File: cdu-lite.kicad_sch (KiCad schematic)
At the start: 0 parts

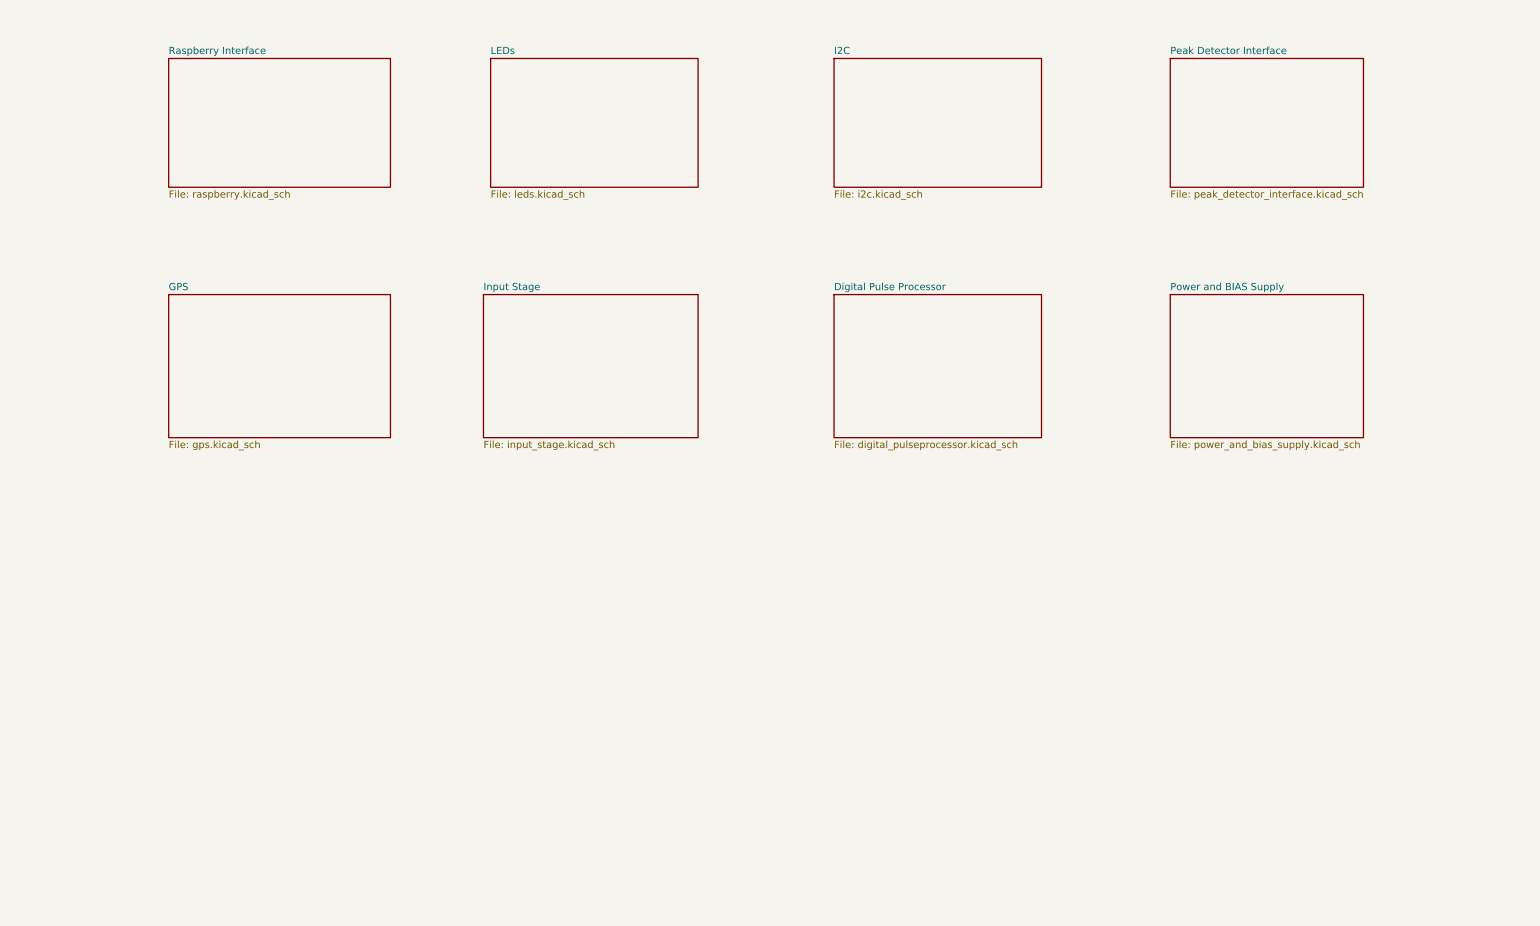
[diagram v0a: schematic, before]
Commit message: Refactored schematic to better show relationship in main schematic
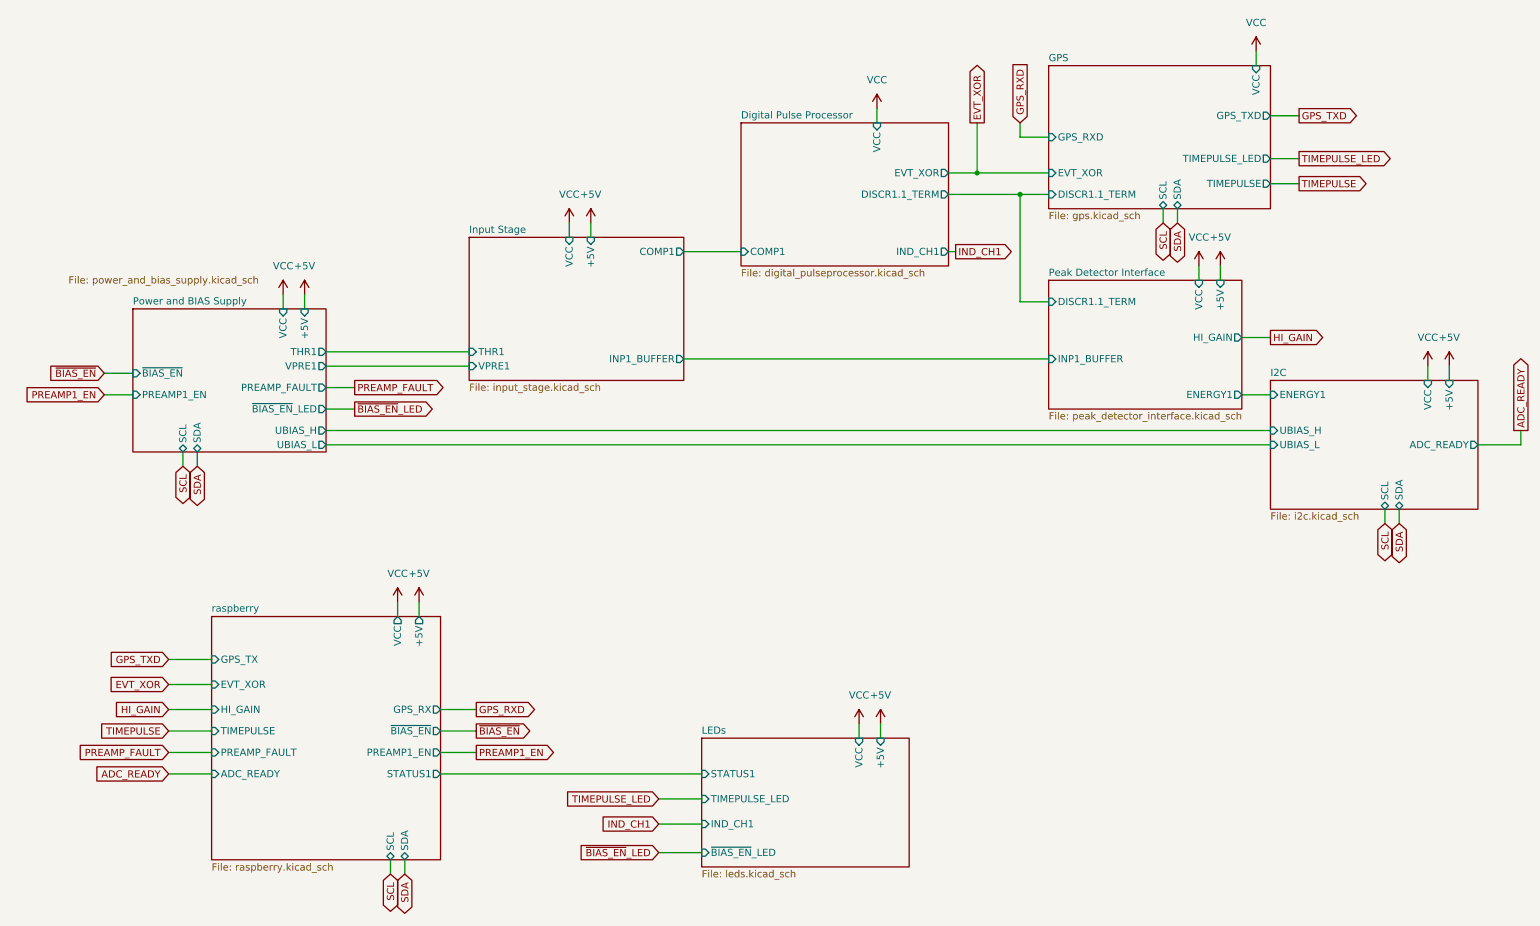
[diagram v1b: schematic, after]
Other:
- removed sheet Raspberry Interface
- added sheet raspberry (raspberry.kicad_sch)
- sheet Digital Pulse Processor ports: added COMP1, DISCR1.1_TERM, EVT_XOR, IND_CH1, VCC; removed none
- sheet GPS ports: added DISCR1.1_TERM, EVT_XOR, GPS_RXD, GPS_TXD, SCL, SDA, TIMEPULSE, TIMEPULSE_LED, VCC; removed none
- sheet I2C ports: added +5V, ADC_READY, ENERGY1, SCL, SDA, UBIAS_H, UBIAS_L, VCC; removed none
- sheet Input Stage ports: added +5V, COMP1, INP1_BUFFER, THR1, VCC, VPRE1; removed none
- sheet LEDs ports: added +5V, IND_CH1, STATUS1, TIMEPULSE_LED, VCC, ~{BIAS_EN}_LED; removed none
- sheet Peak Detector Interface ports: added +5V, DISCR1.1_TERM, ENERGY1, HI_GAIN, INP1_BUFFER, VCC; removed none
- sheet Power and BIAS Supply ports: added +5V, PREAMP1_EN, PREAMP_FAULT, SCL, SDA, THR1, UBIAS_H, UBIAS_L, VCC, VPRE1, ~{BIAS_EN}, ~{BIAS_EN}_LED; removed none

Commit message: Cleaned up board, replaced GPIO footprint with unshrouded version
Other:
- sheet Digital Pulse Processor ports: added 3V3; removed VCC
- sheet GPS ports: added 3V3; removed VCC
- sheet I2C ports: added 3V3, 5V; removed +5V, VCC
- sheet Input Stage ports: added 3V3, 5V; removed +5V, VCC
- sheet LEDs ports: added 3V3, 5V; removed +5V, VCC
- sheet Peak Detector Interface ports: added 3V3, 5V; removed +5V, VCC
- sheet Power and BIAS Supply ports: added 3V3, 5V; removed +5V, VCC
- sheet raspberry ports: added 3V3, 5V; removed +5V, VCC
